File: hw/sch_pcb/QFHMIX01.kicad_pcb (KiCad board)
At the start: 2 copper layers, 90.9 x 90.9 mm, 205 parts, among them J1 HEADER_1x08, J2 +9V, M1 HOLE, M2 HOLE, M3 HOLE, M4 HOLE, M5 HOLE, M6 HOLE, M7 HOLE, M8 HOLE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

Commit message: Layout improvements.
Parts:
- moved C8 6.60 mm to (145.2, 94.5)
- moved C55 3.36 mm to (183.1, 99.7)
- moved C42 3.13 mm to (168.1, 93.0)
- moved C47 2.72 mm to (139.4, 58.5)
- moved C48 2.71 mm to (181.2, 101.7)
- moved C33 2.67 mm to (141.1, 56.7)
- moved C66 1.87 mm to (147.1, 114.0)
- moved C11 1.82 mm to (154.2, 104.1)
- moved L62 1.79 mm to (187.1, 105.7)
- moved C40 1.78 mm to (188.5, 106.9)
- moved L28 1.78 mm to (184.0, 107.0)
- moved C9 1.70 mm to (151.0, 107.4)
- moved C46 1.70 mm to (185.4, 104.0)
- moved R10 1.69 mm to (152.1, 105.2)
- moved L57 1.63 mm to (181.3, 104.2)
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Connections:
- net Net-(C67-Pad2) renamed /Power/3V3VO
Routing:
- net +5V: track 145.4 -> 189.5 mm, vias 13 -> 16
- net +3V3: track 33.0 -> 66.8 mm
- net GND: track 42.3 -> 21.9 mm, vias 468 -> 456
- net /LNA/QFH_IN_2_N: track 79.1 -> 62.9 mm
- net /Power/3V3VO: track 12.0 -> 18.3 mm
- net /LNA/QFH_IN_2_P: track 76.4 -> 72.1 mm
- net /LNA/QFH_IN_1_N: track 78.8 -> 74.9 mm
- net Net-(C64-Pad2): track 4.18 -> 7.30 mm
- net Net-(C52-Pad2): track 4.65 -> 7.64 mm
- net Net-(C40-Pad1): track 5.88 -> 8.07 mm
- net Net-(C11-Pad1): track 8.08 -> 5.93 mm
- net Net-(C45-Pad1): track 6.42 -> 8.39 mm
- net Net-(L2-Pad1): track 0.00 -> 1.96 mm
- net Net-(C45-Pad2): track 6.51 -> 8.40 mm
- net CLK_IN_P: track 57.0 -> 55.3 mm
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- added copper zone on B.Cu, net /Power/3V3VO

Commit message: Edit PCB
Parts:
- moved C3 0.75 mm to (125.9, 72.0), turned to 45 degrees
- moved C29 0.52 mm to (146.6, 77.3)
- moved C53 0.47 mm to (162.4, 93.3)
- moved L61 0.47 mm to (157.0, 66.8)
- moved L46 0.30 mm to (150.6, 92.8)
- moved C66 0.25 mm to (147.1, 113.8)
- moved L23 0.25 mm to (149.5, 60.3)
- moved L69 0.24 mm to (149.4, 77.3)
- moved L3 0.23 mm to (150.0, 97.0)
- moved L19 0.23 mm to (142.9, 66.9)
- moved L58 0.22 mm to (148.6, 67.4)
- moved C61 0.21 mm to (156.0, 85.9)
- moved L47 0.20 mm to (151.6, 89.8)
- moved C67 0.20 mm to (147.3, 117.0)
- moved C49 0.20 mm to (146.1, 67.3)
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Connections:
- U5 pad 35: (no net) -> GND
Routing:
- net GND: track 21.9 -> 25.4 mm, vias 456 -> 497
- net Net-(C65-Pad1): track 6.54 -> 8.28 mm
- net Net-(C37-Pad1): track 3.61 -> 3.04 mm
- net Net-(C29-Pad1): track 1.78 -> 2.34 mm
- net Net-(C58-Pad1): track 5.87 -> 6.41 mm
- net /Power/3V3VO: track 18.3 -> 18.5 mm, vias 0 -> 18
- added copper zone on F.Cu, net /Power/3V3VO

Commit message: Resolve device package conflicts.
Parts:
- moved C9 2.48 mm to (153.2, 106.4), turned to 45 degrees
- moved L18 2.26 mm to (144.1, 69.7)
- moved C62 1.00 mm to (154.9, 83.8), turned to -135 degrees
- moved C30 0.94 mm to (152.3, 83.4)
- moved C61 0.87 mm to (156.2, 85.0), turned to 45 degrees
- moved C54 0.43 mm to (156.7, 87.9)
- moved L45 0.36 mm to (147.3, 89.8)
- moved L23 0.32 mm to (149.7, 60.1)
- moved C26 0.32 mm to (126.0, 113.5)
- moved L30 0.27 mm to (153.2, 67.9)
- moved C36 0.25 mm to (144.4, 88.1)
- moved L41 0.23 mm to (140.3, 82.4)
- moved L24 0.23 mm to (179.7, 91.1)
- moved L19 0.22 mm to (142.7, 67.1)
- moved C38 0.17 mm to (154.8, 98.2)
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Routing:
- net +5V: track 189.5 -> 186.9 mm, vias 16 -> 12
- net GND: track 25.4 -> 27.8 mm, vias 497 -> 509
- net Net-(L18-Pad1): track 4.33 -> 2.11 mm
- net VCC: track 68.0 -> 69.9 mm
- net Net-(C23-Pad2): track 9.67 -> 8.60 mm
- net Net-(C24-Pad1): track 10.4 -> 9.40 mm
- net Net-(C30-Pad1): track 1.54 -> 2.33 mm
- net Net-(C30-Pad2): track 1.58 -> 2.22 mm

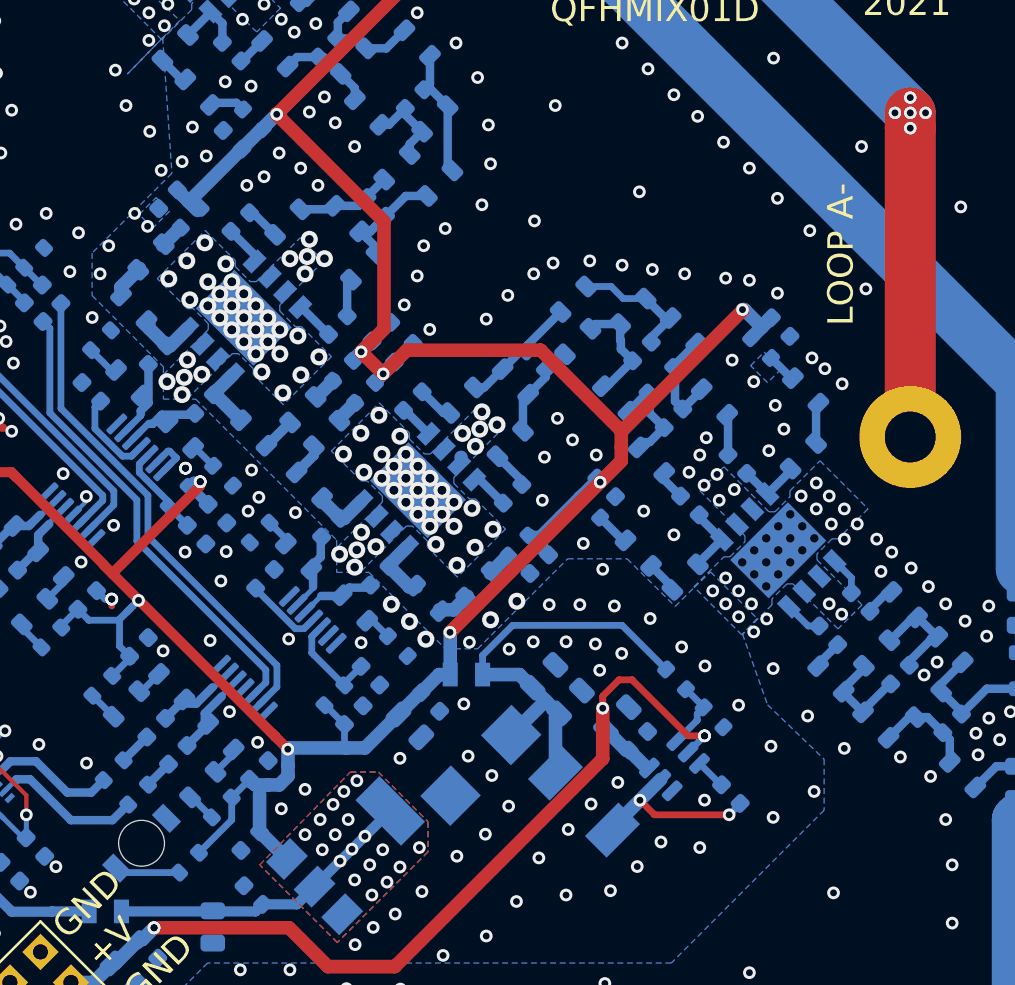
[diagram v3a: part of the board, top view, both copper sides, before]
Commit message: RF layout improvement.
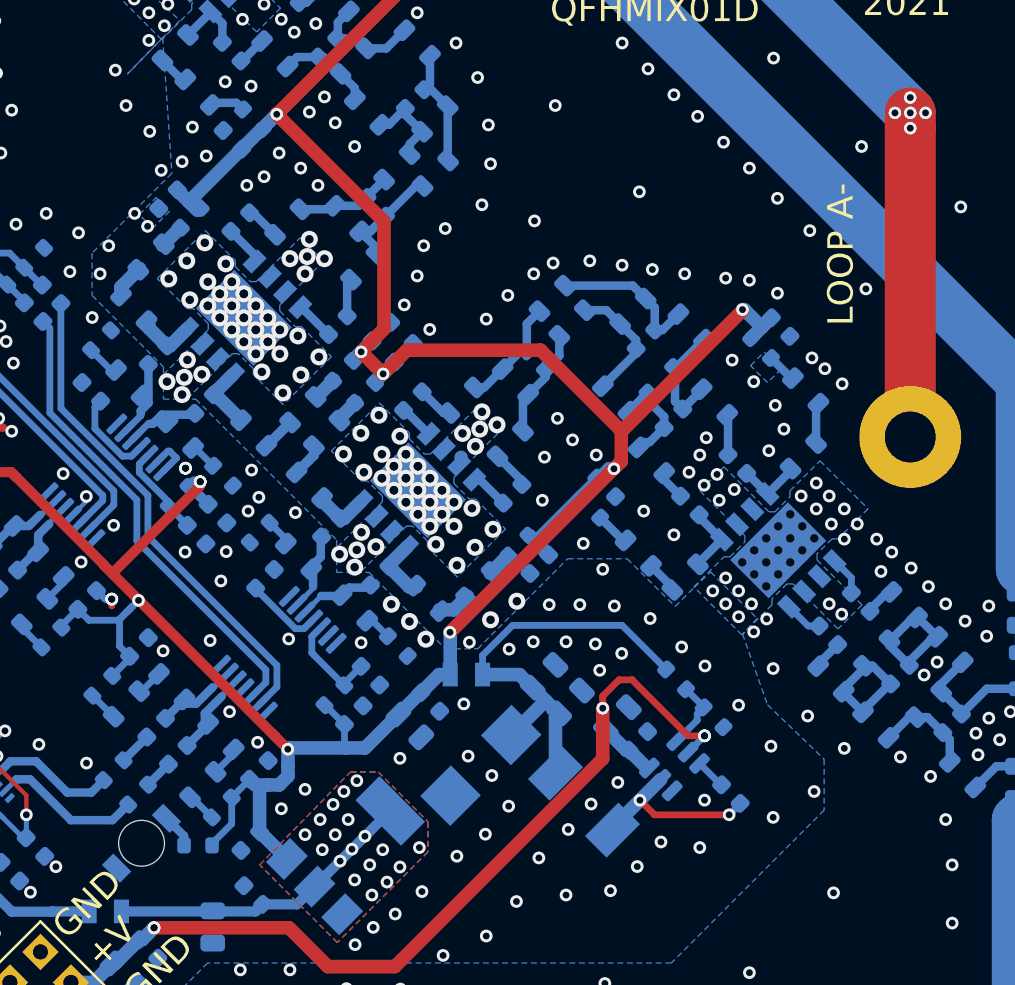
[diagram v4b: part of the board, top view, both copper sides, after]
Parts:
- moved L37 1.25 mm to (164.9, 81.8)
- moved R54 1.15 mm to (144.1, 114.0), turned to 180 degrees
- moved L38 1.14 mm to (166.1, 83.3)
- moved C52 0.74 mm to (170.4, 84.3)
- moved L65 0.64 mm to (158.0, 74.5)
- moved L31 0.51 mm to (173.1, 83.5)
- turned D3 to -135 degrees
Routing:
- net Net-(C46-Pad2): track 6.08 -> 8.10 mm
- net Net-(C46-Pad1): track 6.32 -> 8.28 mm
- net Net-(D3-Pad2): track 3.79 -> 2.02 mm
- net Net-(C52-Pad2): track 7.64 -> 8.92 mm
- net Net-(C64-Pad1): track 5.67 -> 6.48 mm
- net Net-(C63-Pad1): track 7.85 -> 7.16 mm
- net Net-(C52-Pad1): track 6.70 -> 7.27 mm

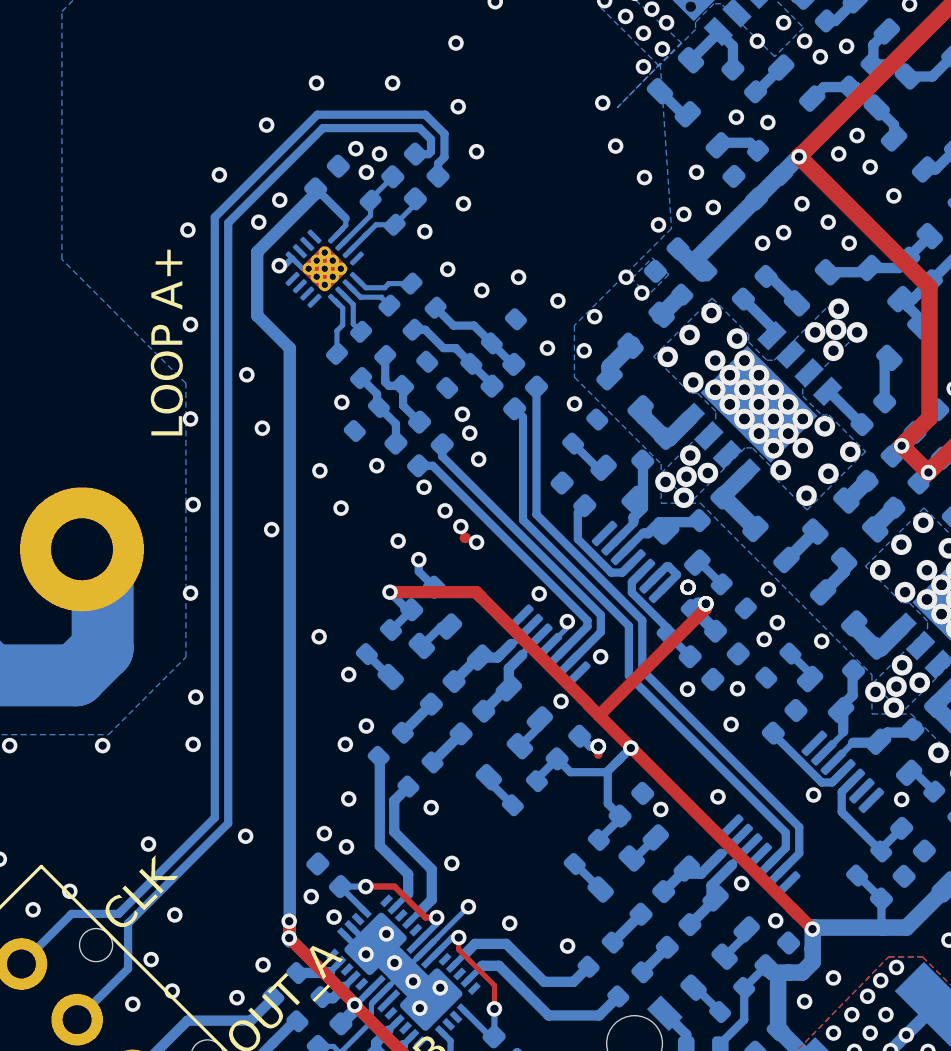
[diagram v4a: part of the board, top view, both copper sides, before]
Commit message: Tune skew lenght.
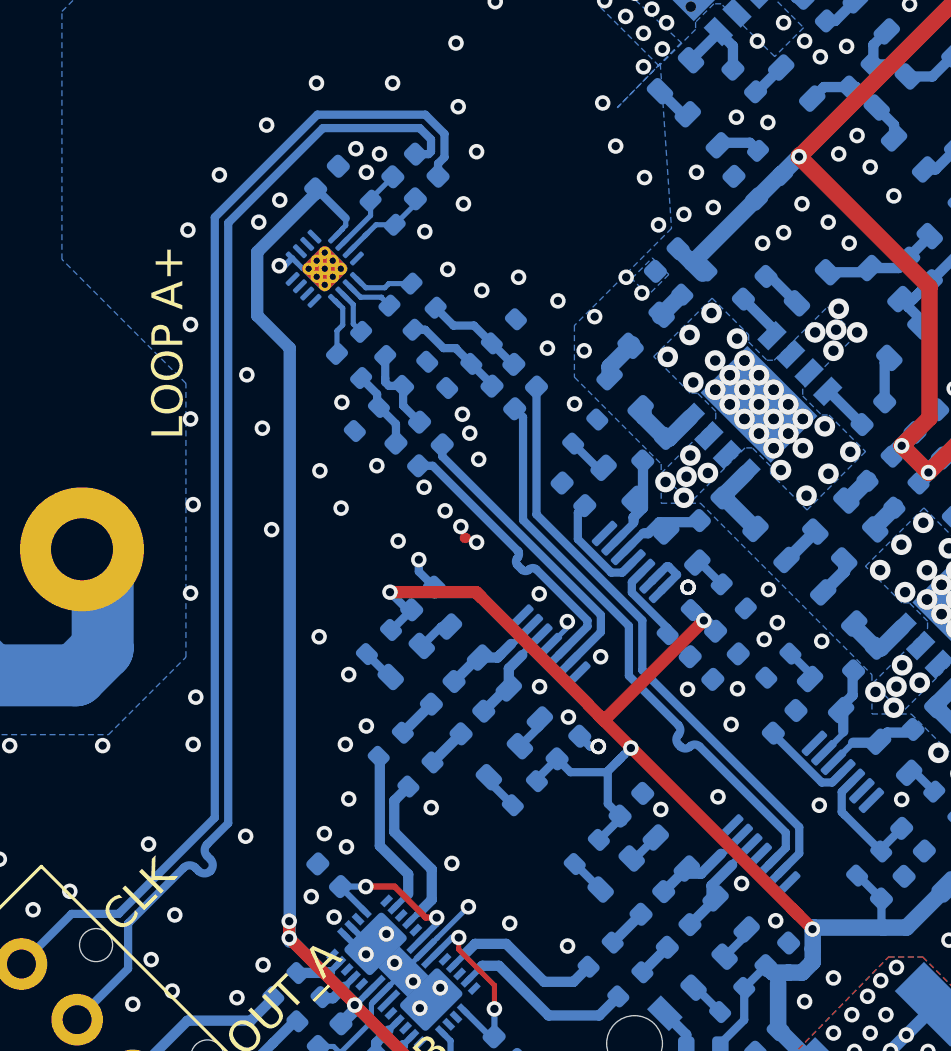
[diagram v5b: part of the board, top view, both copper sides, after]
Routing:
- net CLK_IN_P: track 55.3 -> 56.6 mm
- net /CLK_MIX1_P: track 13.5 -> 14.2 mm
- net /CLK_MIX2_P: track 27.9 -> 28.5 mm
- net +5V: track 186.7 -> 186.3 mm, vias 12 -> 11
- net GND: track 28.1 -> 27.7 mm, vias 509 -> 510

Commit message: Edit PCB
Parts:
- moved C36 0.20 mm to (144.5, 87.9)
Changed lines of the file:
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@@
-(kicad_pcb (version 20210606) (generator pcbnew)
+(kicad_pcb (version 20210228) (generator pcbnew)
   (general
     (thickness 1.6)
@@
   )
   (footprint "Capacitor_SMD:C_0603_1608Metric" (layer "B.Cu")
-    (at 144.4244 88.0618 -135)
-    (descr "Capacitor SMD 0603 (1608 Metric), square (rectangular) end terminal, IPC_7351 nominal, (Body size source: IPC-SM-782 page 76, https://www.pcb-3d.com/wordpress/wp-content/uploads/ipc-sm-782a_amendment_1_and_2.pdf), generated with kicad-footprint-generator")
-    (tags "capacitor")
+    (at 144.526 87.884 -135)
+    (descr "Capacitor SMD 0603 (1608 Metric), square (rectangular) end terminal, IPC_7351 nominal, (Body size source: IPC-SM-782 page 76, https://www.pcb-3d.com/wordpress/wp-content/uploads/ipc-sm-782a_amendment_1_and_2.pdf), generated with kicad-footprint-generator")
+    (tags "capacitor")
